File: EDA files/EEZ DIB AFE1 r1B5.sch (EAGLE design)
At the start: 197 parts, among them IC1 MCP6004T-I/ST, IC10 N.C., IC11 N.C., IC12 N.C., IC13 ADS131E04IPAGR, IC14 TPS71725DCKR, IC15 TPS72325DBVR, IC2 DG212BDY-T1-E3, IC3 ULN2803ADWR, IC4 MCP6004T-I/ST, IC5 DG212BDY-T1-E3, IC6 TLV9001IDBVR, IC7 DG212BDY-T1-E3, IC8 TLV9001IDBVR, IC9 DG212BDY-T1-E3, Q1 CPC3902ZTR, Q2 CPC3902ZTR, Q3 CPC3902ZTR, Q4 CPC3902ZTR, Q5 BSS214NH6327XTSA1, Q6 BSS214NH6327XTSA1, Q7 BSS214NH6327XTSA1, Q8 BSS214NH6327XTSA1, X1 691322310008, X2 DS1023-2*14S21, X3 DS1023-2*14S21

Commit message: #1, #2, BOM (r1B5)
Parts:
- removed C28A: N.C., EEZ_Lib1:C-EU7.5X11
- removed C36, C37, C42, C47, C48: 1u, rcl:C-EUC0805
- removed C38, C39, C40, C41: 470p, rcl:C-EUC0603
- removed C43, C44, C45, C46, C49, C50, C51: 100n, rcl:C-EUC0603
- removed C52: 10u, rcl:C-EUC1206
- removed IC14: TPS71725DCKR, EEZ_TI:TPS71725DCKR
- removed IC15: TPS72325DBVR, EEZ_TI:TPS72325DBVR
- removed JP7: JP2-CUT-0805, EEZ_Lib1:JP2-CUT-0805
- removed R55, R56, R57, R58, R59, R60, R61: 1K, rcl:R-EU_R0805
- removed R62, R63: 10K, rcl:R-EU_R0805
- removed R64, R65: 10R, rcl:R-EU_R1206
- added XO1: N.C., EEZ_DIB:XLH
- C12: value N.C. -> 10u; device rcl:C-EUC0805 -> rcl:C-EUC1206
- C17: value 470p -> 22u; device rcl:C-EUC0603 -> rcl:C-EUC1206
- C18: value 470p -> 10u; device rcl:C-EUC0603 -> rcl:C-EUC1206
- C19: value 470p -> N.C.; device rcl:C-EUC0603 -> EEZ_Lib1:ECAP1206
- C20: value 470p -> N.C.; device rcl:C-EUC0603 -> EEZ_Lib1:C-EU7.5X11
- C21: value 22u -> 100n; device rcl:C-EUC1206 -> rcl:C-EUC0603
- C22: value 10u -> 100n; device rcl:C-EUC1206 -> rcl:C-EUC0603
- C23: value N.C. -> 1u; device rcl:C-EUC0603 -> rcl:C-EUC0805
- C24, C25: value N.C. -> 1u; device rcl:C-EUC1206 -> rcl:C-EUC0805
- C26, C27: value N.C. -> 100n; device rcl:C-EUC1206 -> rcl:C-EUC0603
- C28: value N.C. -> 100n; device EEZ_Lib1:ECAP1206 -> rcl:C-EUC0603
- C29: value N.C. -> 100n
- C30, C31: value 15n -> 1u; device rcl:C-EUC0603 -> rcl:C-EUC0805
- C32, C33: value 15n -> 100n
- C35: value 100n -> 10u; device rcl:C-EUC0603 -> rcl:C-EUC1206
- F3, F5: value ZH32 (10A) -> ZH32 (1.25A)
- F4, F6: value ZH32 (1A) -> ZH32 (10A)
- IC11: value N.C. -> ADS131E04IPAGR; device EEZ_TI:OPA376AIDBVR -> EEZ_TI:ADS131E0XIPAG
- IC12: value N.C. -> TPS71725DCKR; device EEZ_TI:REF50XX -> EEZ_TI:TPS71725DCKR
- IC13: value ADS131E04IPAGR -> TPS72325DBVR; device EEZ_TI:ADS131E0XIPAG -> EEZ_TI:TPS72325DBVR
- R1, R18: value 47R -> 15R
- R33, R43: value 0R33 -> GMR100HTBFIR022; device rcl:R-EU_R1210 -> EEZ_Lib1:R-EU_4WIRE2512
- R51, R52: value N.C. -> 10K
- R53: value N.C. -> 10R; device rcl:R-EU_R0805 -> rcl:R-EU_R1206
- R54: value 1K -> 10R; device rcl:R-EU_R0805 -> rcl:R-EU_R1206
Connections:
- removed net IN1+: C20.2, C30.2, IC13.IN1P, R54.2
- removed net IN1-: C19.2, C30.1, IC13.IN1N, R55.2
- removed net IN2+: C18.2, C31.2, IC13.IN2P, R56.2
- removed net IN2-: C17.2, C31.1, IC13.IN2N, R57.2
- removed net IN3+: C32.2, C38.2, IC13.IN3P, R58.2
- removed net IN3-: C32.1, C39.2, IC13.IN3N, R59.2
- removed net IN4+: C33.2, C40.2, IC13.IN4P, R60.2
- removed net IN4-: C33.1, C41.2, IC13.IN4N, R61.2
- removed net N$100: C27.1, C28.+, C28A.1, IC10.VOUT_F, IC10.VOUT_S, IC12.VOUT, JP5.NC, R53.2
- removed net N$101: C25.1, C26.1, IC11A.+IN, R53.1
- removed net N$102: C12.2, IC11A.-IN, R51.2
- removed net N$103: C12.1, IC11A.OUT, R52.2
- removed net N$104: JP5.NO, R51.1, R52.1
- removed net N$141: F4.2, ISEL10A_1B.NO, ISEL10A_1C.NO
- removed net N$31: F6.2, ISEL10A_2B.NO, ISEL10A_2C.NO
- removed net N$37: F5.2, ISEL10A_2B.COM, ISEL10A_2C.COM
- new net N$2: F6.1, ISEL10A_2B.NC, ISEL10A_2C.NC
- new net N$32: IC9B.D, R43.2S
- new net N$55: Q6.S, R31.1, R33.2
- new net N$97: JP6.NC, XO1.OUT
- net !ADC_CS: now also IC11.!CS; no longer IC13.!CS
- net !ADC_DRDY: now also IC11.!DRDY; no longer IC13.!DRDY
- net !RESET: now also IC11.!RESET; no longer IC13.!RESET
- net +2V5_ADC: now also C25.2, C26.1, C27.1, C28.1, C29.1, C30.2, IC11.AVDD, IC11.AVDD1, IC11.AVDD_2, IC11.AVDD_3, IC11.AVDD_4, IC11.AVDD_5, R53.2; no longer C42.2, C43.1, C44.1, C45.1, C46.1, C47.2, IC13.AVDD, IC13.AVDD1, IC13.AVDD_2, IC13.AVDD_3, IC13.AVDD_4, IC13.AVDD_5, R64.2
- net +2V5_ISO: now also C23.2, IC12.OUT, R53.1; no longer C36.2, IC14.OUT, R64.1
- net +3V3_ISO: now also C31.1, C32.2, C33.2, IC11.DVDD, IC11.DVDD_2, JP5.NC, R51.2, XO1.VDD; no longer C48.1, C49.2, C50.2, IC13.DVDD, IC13.DVDD_2, JP6.NC, R62.2
- net +5V_ISO: now also C12.1; no longer C23.1, C24.1, IC11P.V+, IC12.VIN
- net -2V5_ISO: now also IC13.OUT, R54.2; no longer C25.2, C26.2, C27.2, C28.-, C28A.2, C37.2, IC10.GND, IC12.GND, IC15.OUT, R65.2
- net -5V_ISO: no longer C29.2, IC11P.V-
- net ADC_CLK: now also JP6.NO; no longer JP7.1
- net ADC_MISO: now also IC11.DOUT; no longer IC13.DOUT
- net ADC_MOSI: now also IC11.DIN; no longer IC13.DIN
- net ADC_SCK: now also IC11.SCLK; no longer IC13.SCLK
- net ADC_START: now also IC11.START; no longer IC13.START
- net AIN3P: now also F4.2
- net AIN3P_FUSED: now also F3.1; no longer F4.1
- net AIN4P: now also F5.2, ISEL10A_2B.COM, ISEL10A_2C.COM; no longer F5.1
- net AIN4P_FUSED: now also F5.1; no longer F6.1
- net AVSS: now also C12.2, C17.1, C18.2, C19.-, C20.2, C25.1, C26.2, C29.2, C30.1, C34.1, C35.1, IC10.GND, IC11.AVSS, IC11.AVSS1, IC11.AVSS_2, IC11.AVSS_3, IC11.AVSS_4, IC11.AVSS_5, IC11.VREFN, R54.1; no longer C21.1, C22.2, C42.1, C43.2, C46.2, C47.1, C51.1, C52.1, IC13.AVSS, IC13.AVSS1, IC13.AVSS_2, IC13.AVSS_3, IC13.AVSS_4, IC13.AVSS_5, IC13.VREFN, R65.1
- net GND: now also C21.2, C22.2, C23.1, C24.1, C27.2, C28.2, C31.2, C32.1, C33.1, IC11.DAISY_IN, IC11.DGND, IC11.DGND_2, IC11.DGND_3, IC11.RESV1, IC12.GND, IC13.GND, JP5.NO, XO1.GND; no longer C17.1, C18.1, C19.1, C20.1, C23.2, C29.1, C36.1, C37.1, C38.1, C39.1, C40.1, C41.1, C44.2, C45.2, C48.2, C49.1, C50.1, C51.2, C52.2, IC13.DAISY_IN, IC13.DGND, IC13.DGND_2, IC13.DGND_3, IC13.RESV1, IC14.GND, IC15.GND, JP6.NO
- net HI_CURR#2: now also R33.1S
- net HI_CURR#4: now also F6.2, R43.1S; no longer ISEL10A_2B.NC, ISEL10A_2C.NC
- net IN1N: now also IC11.IN1N; no longer R55.1
- net IN1P: now also IC11.IN1P; no longer R54.1
- net IN2N: now also IC11.IN2N; no longer R57.1
- net IN2P: now also IC11.IN2P; no longer R56.1
- net IN3N: now also IC11.IN3N; no longer R59.1
- net IN3P: now also IC11.IN3P; no longer R58.1
- net IN4N: now also IC11.IN4N; no longer R61.1
- net IN4P: now also IC11.IN4P, IC9B.S, IC9C.D; no longer IC9B.D, IC9C.S, R60.1
- net ISEL_LOW#4: now also IC9C.IN; no longer IC9B.IN
- net ISEL_MID#4: now also IC9B.IN; no longer IC9C.IN
- net N$1: now also IC11.CLKSEL, R52.1; no longer IC13.CLKSEL, R63.1
- net N$14: now also JP5.COM, R52.2; no longer JP6.COM, R63.2
- net N$15: no longer IC9C.D
- net N$17: now also IC9C.S; no longer IC9B.S
- net N$170: now also R33.2S; no longer Q6.S, R31.1, R33.2
- net N$3: now also C21.1, IC12.EN, IC12.IN; no longer C34.1, IC14.EN, IC14.IN
- net N$30: now also F4.1; no longer F3.1
- net N$9: now also C22.1, IC13.EN, IC13.IN; no longer C35.1, IC15.EN, IC15.IN
- net N$92: now also C17.2, IC11.VCAP1; no longer C21.2, IC13.VCAP1
- net N$93: now also IC11.VCAP2; no longer IC13.VCAP2
- net N$94: now also IC11.VCAP3; no longer IC13.VCAP3
- net N$95: now also IC11.VCAP4; no longer IC13.VCAP4
- net N$96: now also IC11.CLK, JP6.COM; no longer IC13.CLK, JP7.2
- net N$98: now also IC11.!PWDN, R51.1; no longer IC13.!PWDN, R62.1
- net VREFP: now also C18.1, C19.+, C20.1, IC10.VOUT_F, IC10.VOUT_S, IC11.VREFP; no longer C22.1, IC13.VREFP, JP5.COM
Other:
- note removed: "Vref buffer (optional)"
- moved on the sheet: C12, C17, C18, C20, C21, C22, C23, C24, C25, C26, C27, C29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

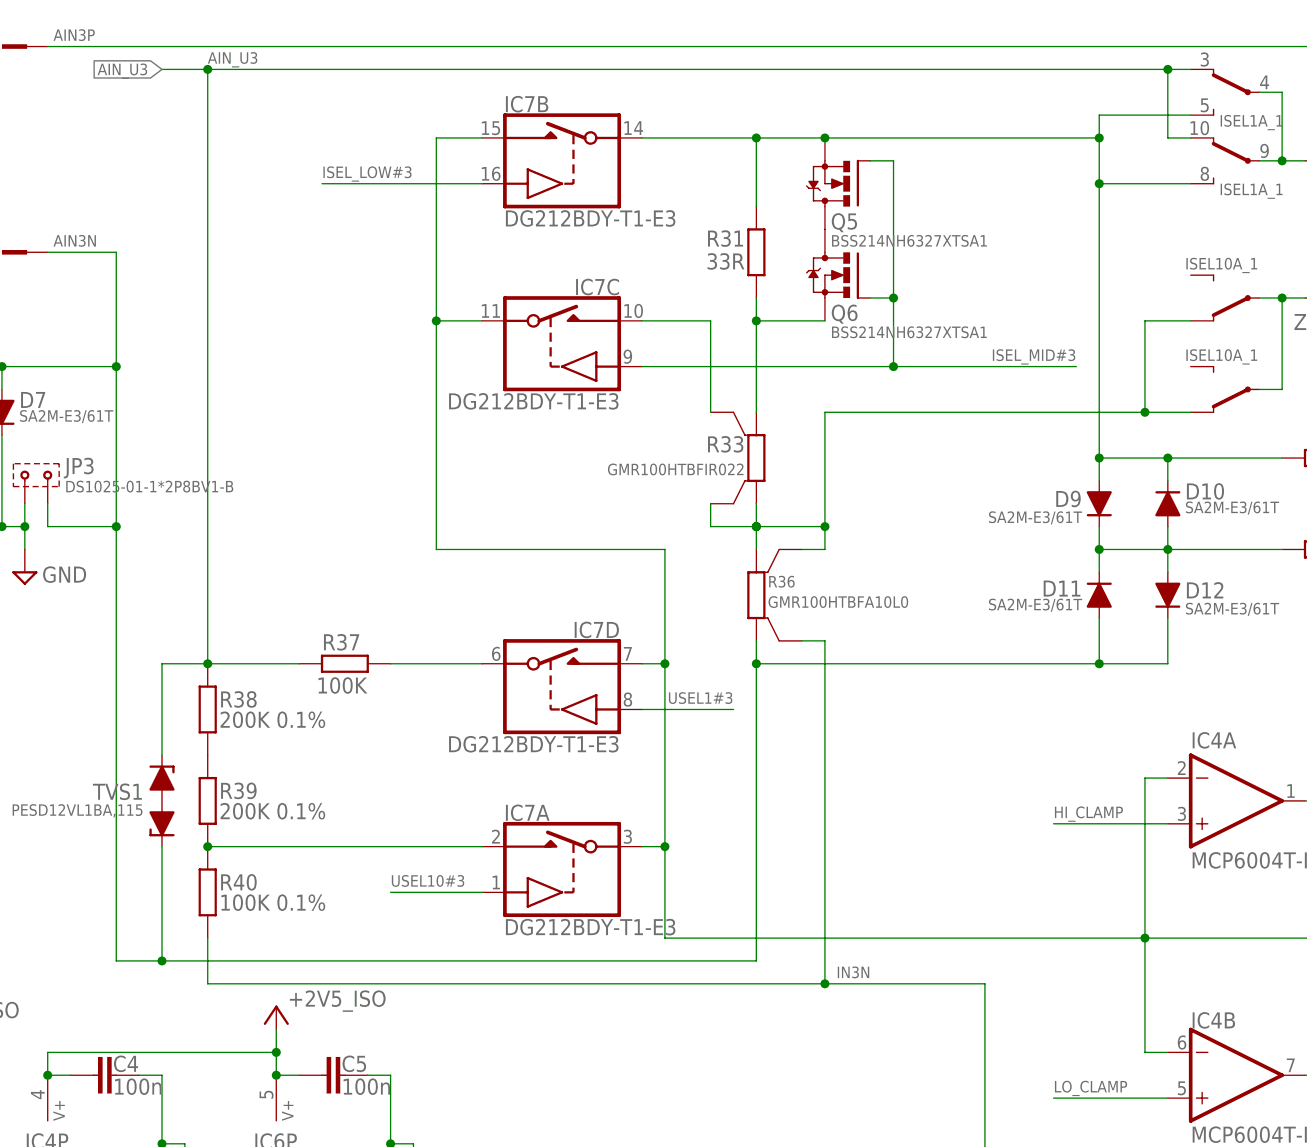
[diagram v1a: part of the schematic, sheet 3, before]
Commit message: New Rsense values, PCB layout adjustment for mid range Rsense
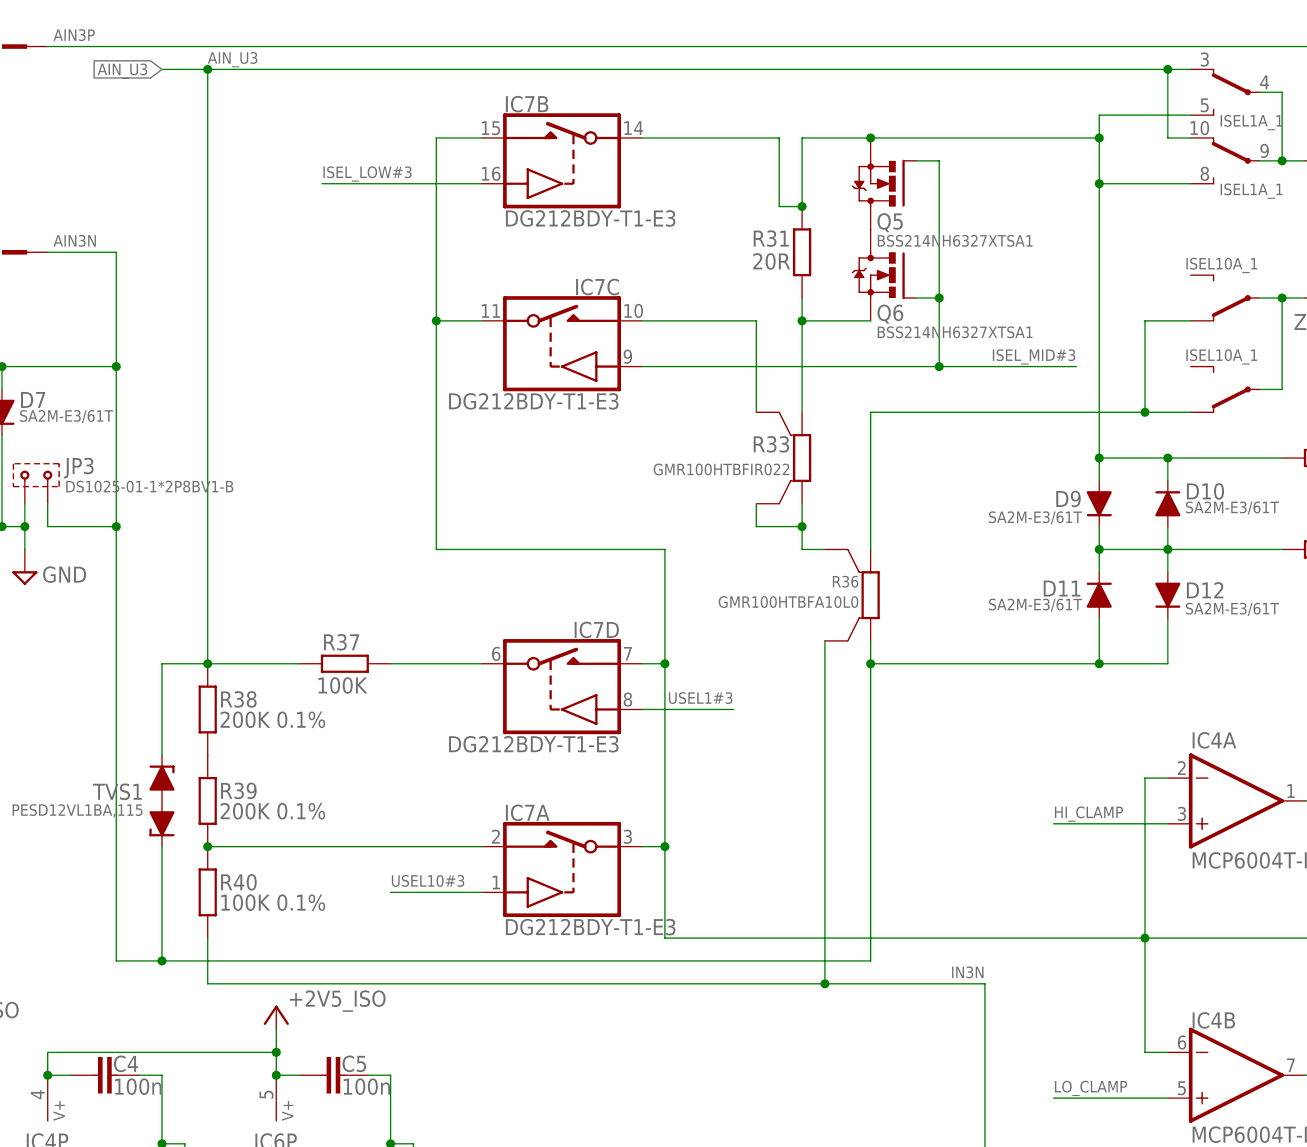
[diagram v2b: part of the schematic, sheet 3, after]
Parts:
- C12: value 10u -> N.C.
- R1, R18: value 15R -> 10R
- R20, R4: value 50R 0.1% -> 33R 0.1%
- R31, R41: value 33R -> 20R
- R53, R54: device rcl:R-EU_R1206 -> rcl:R-EU_R0805
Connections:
- new net N$31: R33.1, R33.1S, R36.2S
- new net N$37: R43.1, R43.1S, R46.2S
- net HI_CURR#2: no longer R33.1, R33.1S, R36.2S
- net HI_CURR#4: no longer R43.1, R43.1S, R46.2S
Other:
- moved on the sheet: Q5, Q6, Q7, Q8, R31, R33, R36, R41, R43, R46
